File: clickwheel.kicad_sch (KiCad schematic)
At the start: 4 parts, among them P2 FPC0.5MM8PPulltypeH2.0mmPickup

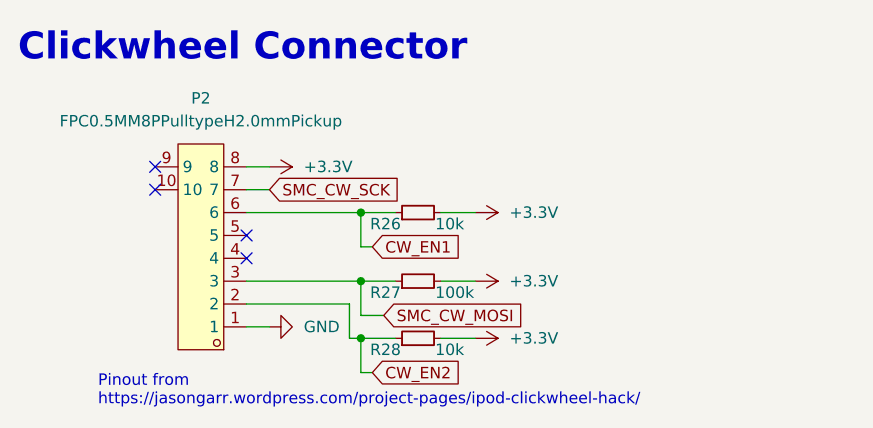
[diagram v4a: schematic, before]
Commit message: schem: migrate away from LCSC exclusive parts
- layout: migrate away from lcsc footprints
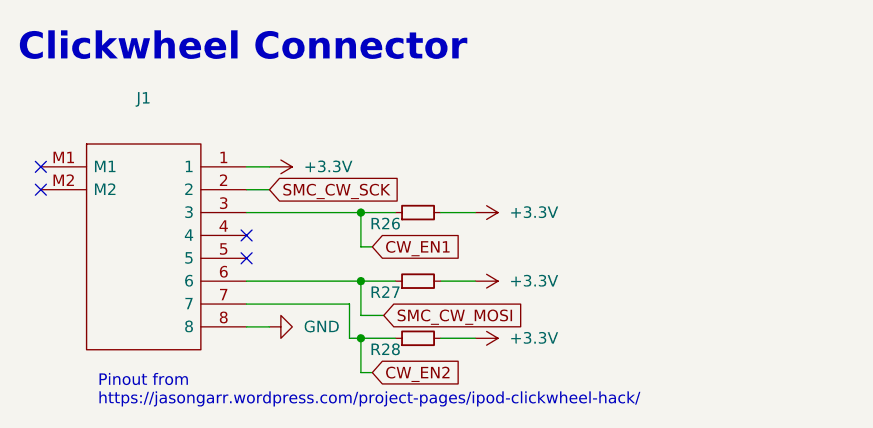
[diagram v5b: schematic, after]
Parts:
- removed P2: FPC0.5MM8PPulltypeH2.0mmPickup, lcsc:FPC-SMD_AFC07-S08ECC-00, symbol lcsc:FPC0.5MM8PPulltypeH2.0mmPickup
- added J1: (no value), symbol gigahawk:SFV8R-2STE1HLF
- R26, R28: value 10k -> (none); footprint Resistor_SMD:R_0402_1005Metric -> (none)
- R27: value 100k -> (none); footprint Resistor_SMD:R_0402_1005Metric -> (none)
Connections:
- net +3V3: now also J1.1
- net CW_EN1: now also J1.3
- net CW_EN2: now also J1.7
- net GND: now also J1.8
- net SMC_CW_MOSI: now also J1.6
- net SMC_CW_SCK: now also J1.2
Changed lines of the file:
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@@
   (junction (at 130.81 101.6) (diameter 0) (color 0 0 0 0)
   )
-  (no_connect (at 107.95 88.9))
-  (no_connect (at 107.95 91.44))
+  (no_connect (at 95.25 88.9))
+  (no_connect (at 95.25 91.44))
   (no_connect (at 118.11 96.52))
   (no_connect (at 118.11 99.06))
@@
     )
   )
-  (symbol (lib_id "lcsc:FPC0.5MM8PPulltypeH2.0mmPickup") (at 114.3 97.79 180) (unit 1)
-    (in_bom yes) (on_board yes) (fields_autoplaced)
-    (property "Reference" "P2" (id 0) (at 113.03 81.28 0))
-    (property "Value" "FPC0.5MM8PPulltypeH2.0mmPickup" (id 1) (at 113.03 83.82 0))
-    (property "Footprint" "lcsc:FPC-SMD_AFC07-S08ECC-00" (id 2) (at 114.3 81.28 0)
-      (effects (font (size 1.27 1.27)) hide)
-    )
-    (property "Datasheet" "https://lcsc.com/product-detail/FPC-Connectors_FPC-0-5mmpitch-8P-H2-0mm-Pull-type-Pick-up_C11084.html" (id 3) (at 114.3 78.74 0)
-      (effects (font (size 1.27 1.27)) hide)
-    )
-    (property "Manufacturer" "ReliaPro" (id 4) (at 114.3 76.2 0)
-      (effects (font (size 1.27 1.27)) hide)
-    )
-    (property "LCSC Part" "C11084" (id 5) (at 114.3 73.66 0)
-      (effects (font (size 1.27 1.27)) hide)
-    )
-    (property "JLC Part" "Extended Part" (id 6) (at 114.3 71.12 0)
-      (effects (font (size 1.27 1.27)) hide)
-    )
-    (pin "1")
-    (pin "10")
+  (symbol (lib_id "power:+3.3V") (at 143.51 93.98 270) (unit 1)
+    (in_bom yes) (on_board yes) (fields_autoplaced)
+    (property "Reference" "#PWR063" (id 0) (at 139.7 93.98 0)
+      (effects (font (size 1.27 1.27)) hide)
+    )
+    (property "Value" "+3.3V" (id 1) (at 147.32 93.9799 90)
+      (effects (font (size 1.27 1.27)) (justify left))
+    )
+    (property "Footprint" "" (id 2) (at 143.51 93.98 0)
+      (effects (font (size 1.27 1.27)) hide)
+    )
+    (property "Datasheet" "" (id 3) (at 143.51 93.98 0)
+      (effects (font (size 1.27 1.27)) hide)
+    )
+    (pin "1")
+  )
+  (symbol (lib_id "power:GND") (at 120.65 106.68 90) (unit 1)
+    (in_bom yes) (on_board yes) (fields_autoplaced)
+    (property "Reference" "#PWR062" (id 0) (at 127 106.68 0)
+      (effects (font (size 1.27 1.27)) hide)
+    )
+    (property "Value" "GND" (id 1) (at 124.46 106.6799 90)
+      (effects (font (size 1.27 1.27)) (justify right))
+    )
+    (property "Footprint" "" (id 2) (at 120.65 106.68 0)
+      (effects (font (size 1.27 1.27)) hide)
+    )
+    (property "Datasheet" "" (id 3) (at 120.65 106.68 0)
+      (effects (font (size 1.27 1.27)) hide)
+    )
+    (pin "1")
+  )
+  (symbol (lib_id "gigahawk:SFV8R-2STE1HLF") (at 95.25 88.9 0) (unit 1)
+    (in_bom yes) (on_board yes) (fields_autoplaced)
+    (property "Reference" "J1" (id 0) (at 106.68 81.28 0))
+    (property "Value" "" (id 1) (at 106.68 83.82 0))
+    (property "Footprint" "" (id 2) (at 114.3 86.36 0)
+      (effects (font (size 1.27 1.27)) (justify left) hide)
+    )
+    (property "Datasheet" "https://cdn.amphenol-icc.com/media/wysiwyg/files/drawing/10112793.pdf" (id 3) (at 114.3 88.9 0)
+      (effects (font (size 1.27 1.27)) (justify left) hide)
+    )
+    (property "Description" "FFC & FPC Connectors FFC/FPC CONN" (id 4) (at 114.3 91.44 0)
+      (effects (font (size 1.27 1.27)) (justify left) hide)
+    )
+    (property "Height" "2" (id 5) (at 114.3 93.98 0)
+      (effects (font (size 1.27 1.27)) (justify left) hide)
+    )
+    (property "Mouser Price/Stock" "https://www.mouser.co.uk/ProductDetail/Amphenol-FCI/SFV8R-2STE1HLF?qs=SqJKR5Mmryfw9HHOb%2F1Fzg%3D%3D" (id 7) (at 114.3 99.06 0)
+      (effects (font (size 1.27 1.27)) (justify left) hide)
+    )
+    (property "Manufacturer" "Amphenol" (id 10) (at 114.3 101.6 0)
+      (effects (font (size 1.27 1.27)) (justify left) hide)
+    )
+    (property "Digikey Price/Stock" "https://www.digikey.com/en/products/detail/amphenol-cs-fci/SFV8R-2STE1HLF/2626755" (id 13) (at 95.25 88.9 0)
+      (effects (font (size 1.27 1.27)) hide)
+    )
+    (property "Mouser Part" "649-SFV8R-2STE1HLF" (id 9) (at 114.3 96.52 0)
+      (effects (font (size 1.27 1.27)) (justify left) hide)
+    )
+    (property "Manufacturer Part" "SFV8R-2STE1HLF" (id 14) (at 114.3 104.14 0)
+      (effects (font (size 1.27 1.27)) (justify left) hide)
+    )
+    (property "Digikey Part" "609-4334-1-ND" (id 11) (at 95.25 88.9 0)
+      (effects (font (size 1.27 1.27)) hide)
+    )
+    (pin "1")
     (pin "2")
     (pin "3")
@@
     (pin "7")
     (pin "8")
-    (pin "9")
-  )
-  (symbol (lib_id "power:+3.3V") (at 143.51 93.98 270) (unit 1)
-    (in_bom yes) (on_board yes) (fields_autoplaced)
-    (property "Reference" "#PWR063" (id 0) (at 139.7 93.98 0)
-      (effects (font (size 1.27 1.27)) hide)
-    )
-    (property "Value" "+3.3V" (id 1) (at 147.32 93.9799 90)
-      (effects (font (size 1.27 1.27)) (justify left))
-    )
-    (property "Footprint" "" (id 2) (at 143.51 93.98 0)
-      (effects (font (size 1.27 1.27)) hide)
-    )
-    (property "Datasheet" "" (id 3) (at 143.51 93.98 0)
-      (effects (font (size 1.27 1.27)) hide)
-    )
-    (pin "1")
-  )
-  (symbol (lib_id "power:GND") (at 120.65 106.68 90) (unit 1)
-    (in_bom yes) (on_board yes) (fields_autoplaced)
-    (property "Reference" "#PWR062" (id 0) (at 127 106.68 0)
-      (effects (font (size 1.27 1.27)) hide)
-    )
-    (property "Value" "GND" (id 1) (at 124.46 106.6799 90)
-      (effects (font (size 1.27 1.27)) (justify right))
-    )
-    (property "Footprint" "" (id 2) (at 120.65 106.68 0)
-      (effects (font (size 1.27 1.27)) hide)
-    )
-    (property "Datasheet" "" (id 3) (at 120.65 106.68 0)
-      (effects (font (size 1.27 1.27)) hide)
-    )
-    (pin "1")
+    (pin "M1")
+    (pin "M2")
   )
   (symbol (lib_id "Device:R_Small") (at 137.16 93.98 90) (unit 1)
@@
       (effects (font (size 1.27 1.27)) (justify left))
     )
-    (property "Value" "10k" (id 1) (at 139.065 95.25 90)
-      (effects (font (size 1.27 1.27)) (justify right))
-    )
-    (property "Footprint" "Resistor_SMD:R_0402_1005Metric" (id 2) (at 137.16 93.98 0)
+    (property "Value" "" (id 1) (at 139.065 95.25 90)
+      (effects (font (size 1.27 1.27)) (justify right))
+    )
+    (property "Footprint" "" (id 2) (at 137.16 93.98 0)
       (effects (font (size 1.27 1.27)) hide)
     )
@@
       (effects (font (size 1.27 1.27)) (justify left))
     )
-    (property "Value" "10k" (id 1) (at 139.065 109.22 90)
-      (effects (font (size 1.27 1.27)) (justify right))
-    )
-    (property "Footprint" "Resistor_SMD:R_0402_1005Metric" (id 2) (at 137.16 107.95 0)
+    (property "Value" "" (id 1) (at 139.065 109.22 90)
+      (effects (font (size 1.27 1.27)) (justify right))
+    )
+    (property "Footprint" "" (id 2) (at 137.16 107.95 0)
       (effects (font (size 1.27 1.27)) hide)
     )
@@
       (effects (font (size 1.27 1.27)) (justify left))
     )
-    (property "Value" "100k" (id 1) (at 139.065 102.87 90)
-      (effects (font (size 1.27 1.27)) (justify right))
-    )
-    (property "Footprint" "Resistor_SMD:R_0402_1005Metric" (id 2) (at 137.16 101.6 0)
-      (effects (font (size 1.27 1.27)) hide)
-    )
+    (property "Value" "" (id 1) (at 139.065 102.87 90)
+      (effects (font (size 1.27 1.27)) (justify right))
+    )
+    (property "Footprint" "" (id 2) (at 137.16 101.6 0)
+      (effects (font (size 1.27 1.27)) hide)
+    )

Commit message: layout: update footprint for TP4056M
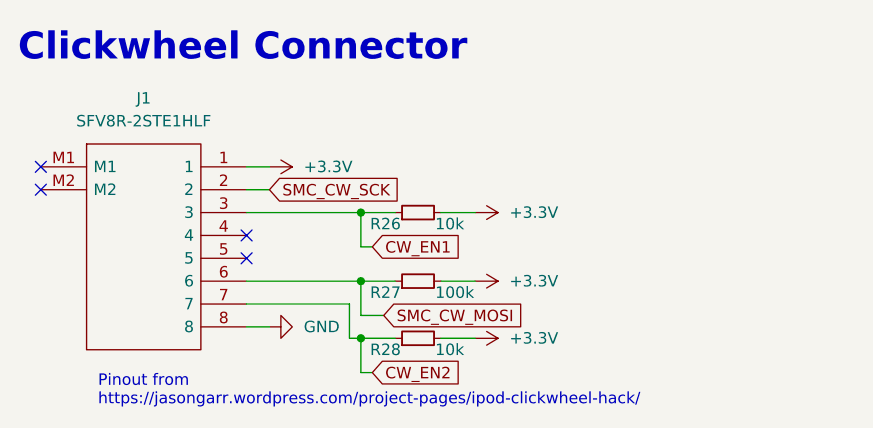
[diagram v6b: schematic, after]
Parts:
- J1: value (none) -> SFV8R-2STE1HLF; footprint (none) -> Gigahawk:SFV8R2STE1HLF
- R26, R28: value (none) -> 10k; footprint (none) -> Resistor_SMD:R_0402_1005Metric
- R27: value (none) -> 100k; footprint (none) -> Resistor_SMD:R_0402_1005Metric
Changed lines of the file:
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@@
     (in_bom yes) (on_board yes) (fields_autoplaced)
     (property "Reference" "J1" (id 0) (at 106.68 81.28 0))
-    (property "Value" "" (id 1) (at 106.68 83.82 0))
-    (property "Footprint" "" (id 2) (at 114.3 86.36 0)
+    (property "Value" "SFV8R-2STE1HLF" (id 1) (at 106.68 83.82 0))
+    (property "Footprint" "Gigahawk:SFV8R2STE1HLF" (id 2) (at 114.3 86.36 0)
       (effects (font (size 1.27 1.27)) (justify left) hide)
     )
@@
       (effects (font (size 1.27 1.27)) (justify left))
     )
-    (property "Value" "" (id 1) (at 139.065 95.25 90)
+    (property "Value" "10k" (id 1) (at 139.065 95.25 90)
       (effects (font (size 1.27 1.27)) (justify right))
     )
-    (property "Footprint" "" (id 2) (at 137.16 93.98 0)
+    (property "Footprint" "Resistor_SMD:R_0402_1005Metric" (id 2) (at 137.16 93.98 0)
       (effects (font (size 1.27 1.27)) hide)
     )
@@
       (effects (font (size 1.27 1.27)) (justify left))
     )
-    (property "Value" "" (id 1) (at 139.065 109.22 90)
+    (property "Value" "10k" (id 1) (at 139.065 109.22 90)
       (effects (font (size 1.27 1.27)) (justify right))
     )
-    (property "Footprint" "" (id 2) (at 137.16 107.95 0)
+    (property "Footprint" "Resistor_SMD:R_0402_1005Metric" (id 2) (at 137.16 107.95 0)
       (effects (font (size 1.27 1.27)) hide)
     )
@@
       (effects (font (size 1.27 1.27)) (justify left))
     )
-    (property "Value" "" (id 1) (at 139.065 102.87 90)
+    (property "Value" "100k" (id 1) (at 139.065 102.87 90)
       (effects (font (size 1.27 1.27)) (justify right))
     )
-    (property "Footprint" "" (id 2) (at 137.16 101.6 0)
+    (property "Footprint" "Resistor_SMD:R_0402_1005Metric" (id 2) (at 137.16 101.6 0)
       (effects (font (size 1.27 1.27)) hide)
     )

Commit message: layout: preliminary layout of most of board
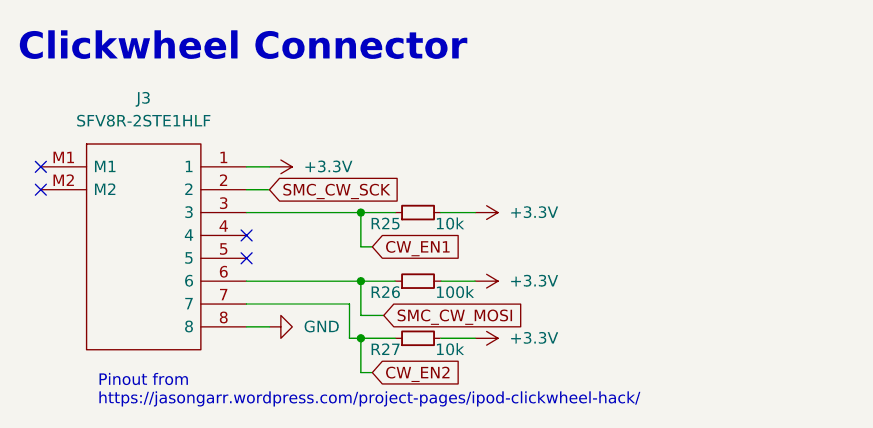
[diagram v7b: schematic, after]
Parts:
- renumbered J1 to J3, R26 to R25, R27 to R26, R28 to R27
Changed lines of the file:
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@@
   (symbol (lib_id "power:+3.3V") (at 143.51 93.98 270) (unit 1)
     (in_bom yes) (on_board yes) (fields_autoplaced)
-    (property "Reference" "#PWR063" (id 0) (at 139.7 93.98 0)
+    (property "Reference" "#PWR066" (id 0) (at 139.7 93.98 0)
       (effects (font (size 1.27 1.27)) hide)
     )
@@
   (symbol (lib_id "power:GND") (at 120.65 106.68 90) (unit 1)
     (in_bom yes) (on_board yes) (fields_autoplaced)
-    (property "Reference" "#PWR062" (id 0) (at 127 106.68 0)
+    (property "Reference" "#PWR065" (id 0) (at 127 106.68 0)
       (effects (font (size 1.27 1.27)) hide)
     )
@@
   (symbol (lib_id "gigahawk:SFV8R-2STE1HLF") (at 95.25 88.9 0) (unit 1)
     (in_bom yes) (on_board yes) (fields_autoplaced)
-    (property "Reference" "J1" (id 0) (at 106.68 81.28 0))
+    (property "Reference" "J3" (id 0) (at 106.68 81.28 0))
     (property "Value" "SFV8R-2STE1HLF" (id 1) (at 106.68 83.82 0))
     (property "Footprint" "Gigahawk:SFV8R2STE1HLF" (id 2) (at 114.3 86.36 0)
@@
   (symbol (lib_id "Device:R_Small") (at 137.16 93.98 90) (unit 1)
     (in_bom yes) (on_board yes)
-    (property "Reference" "R26" (id 0) (at 135.255 95.25 90)
+    (property "Reference" "R25" (id 0) (at 135.255 95.25 90)
       (effects (font (size 1.27 1.27)) (justify left))
     )
@@
   (symbol (lib_id "Device:R_Small") (at 137.16 107.95 90) (unit 1)
     (in_bom yes) (on_board yes)
-    (property "Reference" "R28" (id 0) (at 135.255 109.22 90)
+    (property "Reference" "R27" (id 0) (at 135.255 109.22 90)
       (effects (font (size 1.27 1.27)) (justify left))
     )
@@
   (symbol (lib_id "power:+3.3V") (at 120.65 88.9 270) (unit 1)
     (in_bom yes) (on_board yes) (fields_autoplaced)
-    (property "Reference" "#PWR061" (id 0) (at 116.84 88.9 0)
+    (property "Reference" "#PWR064" (id 0) (at 116.84 88.9 0)
       (effects (font (size 1.27 1.27)) hide)
     )
@@
   (symbol (lib_id "power:+3.3V") (at 143.51 101.6 270) (unit 1)
     (in_bom yes) (on_board yes) (fields_autoplaced)
-    (property "Reference" "#PWR064" (id 0) (at 139.7 101.6 0)
+    (property "Reference" "#PWR067" (id 0) (at 139.7 101.6 0)
       (effects (font (size 1.27 1.27)) hide)
     )
@@
   (symbol (lib_id "power:+3.3V") (at 143.51 107.95 270) (unit 1)
     (in_bom yes) (on_board yes) (fields_autoplaced)
-    (property "Reference" "#PWR065" (id 0) (at 139.7 107.95 0)
+    (property "Reference" "#PWR068" (id 0) (at 139.7 107.95 0)
       (effects (font (size 1.27 1.27)) hide)
     )
@@
   (symbol (lib_id "Device:R_Small") (at 137.16 101.6 90) (unit 1)
     (in_bom yes) (on_board yes)
-    (property "Reference" "R27" (id 0) (at 135.255 102.87 90)
+    (property "Reference" "R26" (id 0) (at 135.255 102.87 90)
       (effects (font (size 1.27 1.27)) (justify left))
     )

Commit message: layout, routing: relayout and reroute board
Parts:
- J3: value SFV8R-2STE1HLF -> (none); footprint Gigahawk:SFV8R2STE1HLF -> (none)
- R25, R27: value 10k -> (none); footprint Resistor_SMD:R_0402_1005Metric -> (none)
- R26: value 100k -> (none); footprint Resistor_SMD:R_0402_1005Metric -> (none)
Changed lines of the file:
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@@
     (in_bom yes) (on_board yes) (fields_autoplaced)
     (property "Reference" "J3" (id 0) (at 106.68 81.28 0))
-    (property "Value" "SFV8R-2STE1HLF" (id 1) (at 106.68 83.82 0))
-    (property "Footprint" "Gigahawk:SFV8R2STE1HLF" (id 2) (at 114.3 86.36 0)
+    (property "Value" "" (id 1) (at 106.68 83.82 0))
+    (property "Footprint" "" (id 2) (at 114.3 86.36 0)
       (effects (font (size 1.27 1.27)) (justify left) hide)
     )
@@
       (effects (font (size 1.27 1.27)) (justify left))
     )
-    (property "Value" "10k" (id 1) (at 139.065 95.25 90)
+    (property "Value" "" (id 1) (at 139.065 95.25 90)
       (effects (font (size 1.27 1.27)) (justify right))
     )
-    (property "Footprint" "Resistor_SMD:R_0402_1005Metric" (id 2) (at 137.16 93.98 0)
+    (property "Footprint" "" (id 2) (at 137.16 93.98 0)
       (effects (font (size 1.27 1.27)) hide)
     )
@@
       (effects (font (size 1.27 1.27)) (justify left))
     )
-    (property "Value" "10k" (id 1) (at 139.065 109.22 90)
+    (property "Value" "" (id 1) (at 139.065 109.22 90)
       (effects (font (size 1.27 1.27)) (justify right))
     )
-    (property "Footprint" "Resistor_SMD:R_0402_1005Metric" (id 2) (at 137.16 107.95 0)
+    (property "Footprint" "" (id 2) (at 137.16 107.95 0)
       (effects (font (size 1.27 1.27)) hide)
     )
@@
       (effects (font (size 1.27 1.27)) (justify left))
     )
-    (property "Value" "100k" (id 1) (at 139.065 102.87 90)
+    (property "Value" "" (id 1) (at 139.065 102.87 90)
       (effects (font (size 1.27 1.27)) (justify right))
     )
-    (property "Footprint" "Resistor_SMD:R_0402_1005Metric" (id 2) (at 137.16 101.6 0)
+    (property "Footprint" "" (id 2) (at 137.16 101.6 0)
       (effects (font (size 1.27 1.27)) hide)
     )
